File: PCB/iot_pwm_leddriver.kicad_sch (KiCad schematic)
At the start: 17 parts, among them J1 ProgConn-SOICBite, J2 12V PWR, SW1 RESET, SW2 FLASH, U2 ESP-12F

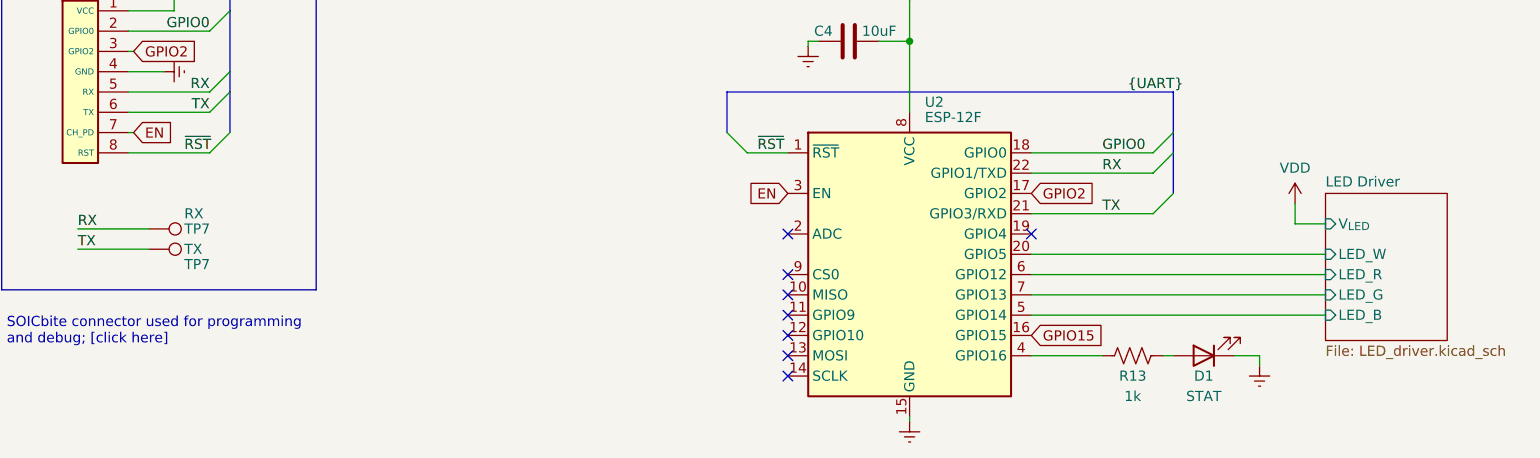
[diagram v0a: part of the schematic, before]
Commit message: design v1.0 - complete redesign
* redid schematic
* changed to screw terminal
* added W channel for RGBW strips
* did layout
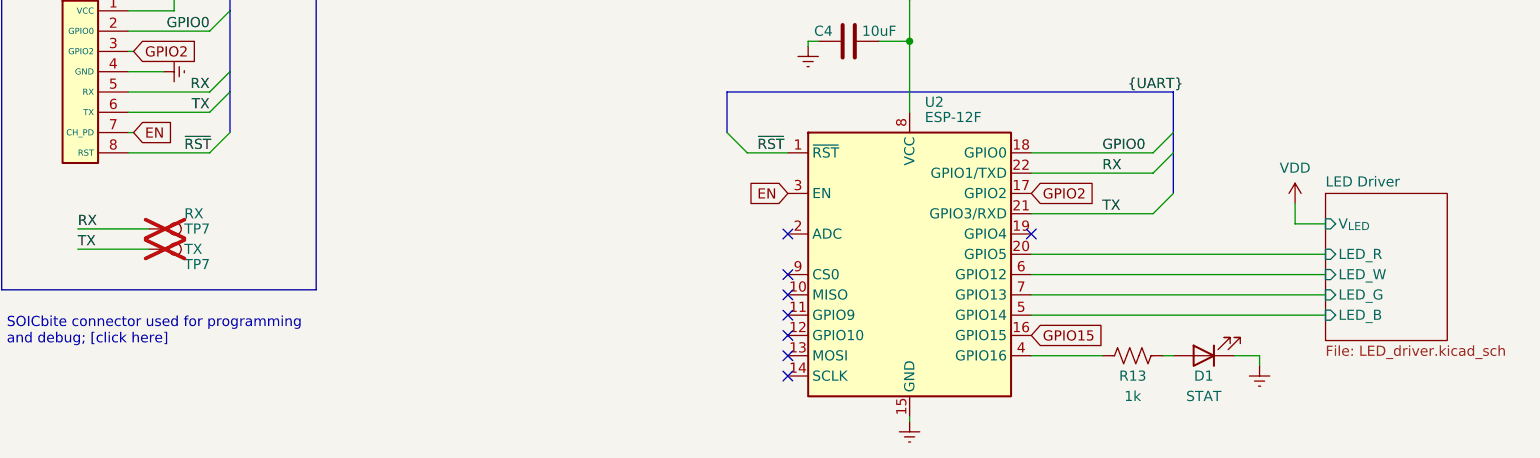
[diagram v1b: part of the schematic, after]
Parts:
- J1: LCSC (none) -> -
- R12, R13: LCSC (none) -> C17513
- TP7: LCSC (none) -> -; now not fitted
- U2: LCSC (none) -> C82891
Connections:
- net LED Driver/LED_R: now also U2.20 (GPIO5); no longer U2.6 (GPIO12)
- net LED Driver/LED_W: now also U2.6 (GPIO12); no longer U2.20 (GPIO5)
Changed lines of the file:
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@@
   )
   (symbol (lib_id "Connector:TestPoint") (at 38.1 113.03 270) (unit 1)
-    (in_bom no) (on_board yes) (dnp no)
+    (in_bom no) (on_board no) (dnp yes)
     (property "Reference" "TP7" (at 42.545 114.935 90)
       (effects (font (size 1.27 1.27)) (justify left))
@@
     )
     (property "Vendor" "~" (at 38.1 113.03 0)
+      (effects (font (size 1.27 1.27)) hide)
+    )
+    (property "Sim.Enable" "0" (at 38.1 113.03 0)
+      (effects (font (size 1.27 1.27)) hide)
+    )
+    (property "LCSC" "-" (at 38.1 113.03 0)
       (effects (font (size 1.27 1.27)) hide)
     )
@@
         )
       )
-      (project "dumb-led-driver"
+      (project "iot_pwm_leddriver"
         (path "/b6358773-9a18-4eb2-bc1b-d38393a8df39/ff2d7abe-3ed9-4cf8-a089-c3975f855094"
           (reference "TP2") (unit 1)
@@
         )
       )
-      (project "dumb-led-driver"
+      (project "iot_pwm_leddriver"
         (path "/b6358773-9a18-4eb2-bc1b-d38393a8df39"
           (reference "#PWR07") (unit 1)
@@
         )
       )
-      (project "dumb-led-driver"
+      (project "iot_pwm_leddriver"
         (path "/b6358773-9a18-4eb2-bc1b-d38393a8df39"
           (reference "#PWR01") (unit 1)
@@
         )
       )
-      (project "dumb-led-driver"
+      (project "iot_pwm_leddriver"
         (path "/b6358773-9a18-4eb2-bc1b-d38393a8df39"
           (reference "#PWR04") (unit 1)
@@
         )
       )
-      (project "dumb-led-driver"
+      (project "iot_pwm_leddriver"
         (path "/b6358773-9a18-4eb2-bc1b-d38393a8df39"
           (reference "#PWR05") (unit 1)
@@
         )
       )
-      (project "dumb-led-driver"
+      (project "iot_pwm_leddriver"
         (path "/b6358773-9a18-4eb2-bc1b-d38393a8df39"
           (reference "#PWR010") (unit 1)
@@
         )
       )
-      (project "dumb-led-driver"
+      (project "iot_pwm_leddriver"
         (path "/b6358773-9a18-4eb2-bc1b-d38393a8df39"
           (reference "#PWR014") (unit 1)
@@
         )
       )
-      (project "dumb-led-driver"
+      (project "iot_pwm_leddriver"
         (path "/b6358773-9a18-4eb2-bc1b-d38393a8df39"
           (reference "D2") (unit 1)
@@
         )
       )
-      (project "dumb-led-driver"
+      (project "iot_pwm_leddriver"
         (path "/b6358773-9a18-4eb2-bc1b-d38393a8df39"
           (reference "#PWR03") (unit 1)
@@
     (pin "1")
     (instances
-      (project "dumb-led-driver"
+      (project "iot_pwm_leddriver"
         (path "/b6358773-9a18-4eb2-bc1b-d38393a8df39"
           (reference "#PWR023") (unit 1)
@@
         )
       )
-      (project "dumb-led-driver"
+      (project "iot_pwm_leddriver"
         (path "/b6358773-9a18-4eb2-bc1b-d38393a8df39"
           (reference "#PWR06") (unit 1)
@@
         )
       )
-      (project "dumb-led-driver"
+      (project "iot_pwm_leddriver"
         (path "/b6358773-9a18-4eb2-bc1b-d38393a8df39"
           (reference "#PWR02") (unit 1)
@@
         )
       )
-      (project "dumb-led-driver"
+      (project "iot_pwm_leddriver"
         (path "/b6358773-9a18-4eb2-bc1b-d38393a8df39"
           (reference "#PWR019") (unit 1)
@@
         )
       )
-      (project "dumb-led-driver"
+      (project "iot_pwm_leddriver"
         (path "/b6358773-9a18-4eb2-bc1b-d38393a8df39"
           (reference "R5") (unit 1)
@@
         )
       )
-      (project "dumb-led-driver"
+      (project "iot_pwm_leddriver"
         (path "/b6358773-9a18-4eb2-bc1b-d38393a8df39"
           (reference "#PWR018") (unit 1)
@@
         )
       )
-      (project "dumb-led-driver"
+      (project "iot_pwm_leddriver"
         (path "/b6358773-9a18-4eb2-bc1b-d38393a8df39"
           (reference "J2") (unit 1)
@@
         )
       )
-      (project "dumb-led-driver"
+      (project "iot_pwm_leddriver"
         (path "/b6358773-9a18-4eb2-bc1b-d38393a8df39"
           (reference "SW1") (unit 1)
@@
         )
       )
-      (project "dumb-led-driver"
+      (project "iot_pwm_leddriver"
         (path "/b6358773-9a18-4eb2-bc1b-d38393a8df39"
           (reference "#PWR017") (unit 1)
@@
         )
       )
-      (project "dumb-led-driver"
+      (project "iot_pwm_leddriver"
         (path "/b6358773-9a18-4eb2-bc1b-d38393a8df39"
           (reference "#PWR021") (unit 1)
@@
         )
       )
-      (project "dumb-led-driver"
+      (project "iot_pwm_leddriver"
         (path "/b6358773-9a18-4eb2-bc1b-d38393a8df39"
           (reference "R2") (unit 1)
@@
         )
       )
-      (project "dumb-led-driver"
+      (project "iot_pwm_leddriver"
         (path "/b6358773-9a18-4eb2-bc1b-d38393a8df39"
           (reference "R3") (unit 1)
@@
         )
       )
-      (project "dumb-led-driver"
+      (project "iot_pwm_leddriver"
         (path "/b6358773-9a18-4eb2-bc1b-d38393a8df39"
           (reference "#PWR09") (unit 1)
@@
         )
       )
-      (project "dumb-led-driver"
+      (project "iot_pwm_leddriver"
         (path "/b6358773-9a18-4eb2-bc1b-d38393a8df39"
           (reference "SW2") (unit 1)
@@
       (effects (font (size 1.27 1.27)) hide)
     )
-    (property "LCSC" "" (at 161.29 126.365 0)
+    (property "LCSC" " C17513 " (at 161.29 126.365 0)
+      (effects (font (size 1.27 1.27)) hide)
+    )
+    (property "Description" "125mW Thick Film Resistors ±100ppm/℃ ±1% 1kΩ 0805 Chip Resistor - Surface Mount ROHS" (at 161.29 126.365 0)
       (effects (font (size 1.27 1.27)) hide)
     )
@@
         )
       )
-      (project "dumb-led-driver"
+      (project "iot_pwm_leddriver"
         (path "/b6358773-9a18-4eb2-bc1b-d38393a8df39"
           (reference "R9") (unit 1)
@@
         )
       )
-      (project "dumb-led-driver"
+      (project "iot_pwm_leddriver"
         (path "/b6358773-9a18-4eb2-bc1b-d38393a8df39"
           (reference "R1") (unit 1)
@@
         )
       )
-      (project "dumb-led-driver"
+      (project "iot_pwm_leddriver"
         (path "/b6358773-9a18-4eb2-bc1b-d38393a8df39"
           (reference "#PWR08") (unit 1)
@@
     )
     (property "Datasheet" "http://wiki.ai-thinker.com/_media/esp8266/esp8266_series_modules_user_manual_v1.1.pdf" (at 124.46 113.665 0)
+      (effects (font (size 1.27 1.27)) hide)
+    )
+    (property "LCSC" " C82891 " (at 133.35 116.205 0)
       (effects (font (size 1.27 1.27)) hide)
     )
@@
         )
       )
-      (project "dumb-led-driver"
+      (project "iot_pwm_leddriver"
         (path "/b6358773-9a18-4eb2-bc1b-d38393a8df39"
           (reference "U1") (unit 1)
@@
   )
   (symbol (lib_id "Connector:TestPoint") (at 38.1 110.49 270) (unit 1)
-    (in_bom no) (on_board yes) (dnp no)
+    (in_bom no) (on_board no) (dnp yes)
     (property "Reference" "TP7" (at 42.545 110.49 90)
       (effects (font (size 1.27 1.27)) (justify left))
@@
     )
     (property "Vendor" "~" (at 38.1 110.49 0)
+      (effects (font (size 1.27 1.27)) hide)
+    )
+    (property "Sim.Enable" "0" (at 38.1 110.49 0)
+      (effects (font (size 1.27 1.27)) hide)
+    )
+    (property "LCSC" "-" (at 38.1 110.49 0)
       (effects (font (size 1.27 1.27)) hide)
     )
@@
         )
       )
-      (project "dumb-led-driver"
+      (project "iot_pwm_leddriver"
         (path "/b6358773-9a18-4eb2-bc1b-d38393a8df39/ff2d7abe-3ed9-4cf8-a089-c3975f855094"
           (reference "TP1") (unit 1)
@@
         )
       )
-      (project "dumb-led-driver"
+      (project "iot_pwm_leddriver"
         (path "/b6358773-9a18-4eb2-bc1b-d38393a8df39"
           (reference "R4") (unit 1)
@@
         )
       )
-      (project "dumb-led-driver"
+      (project "iot_pwm_leddriver"
         (path "/b6358773-9a18-4eb2-bc1b-d38393a8df39"
           (reference "D1") (unit 1)
@@
         )
       )
-      (project "dumb-led-driver"
+      (project "iot_pwm_leddriver"
         (path "/b6358773-9a18-4eb2-bc1b-d38393a8df39"
           (reference "C1") (unit 1)
@@
       (effects (font (size 1.27 1.27)) hide)
     )
-    (property "LCSC" "" (at 93.345 34.925 0)
+    (property "LCSC" " C17513 " (at 93.345 34.925 0)
+      (effects (font (size 1.27 1.27)) hide)
+    )
+    (property "Description" "125mW Thick Film Resistors ±100ppm/℃ ±1% 1kΩ 0805 Chip Resistor - Surface Mount ROHS" (at 93.345 34.925 0)
       (effects (font (size 1.27 1.27)) hide)
     )
@@
         )
       )
-      (project "dumb-led-driver"
+      (project "iot_pwm_leddriver"
         (path "/b6358773-9a18-4eb2-bc1b-d38393a8df39"
           (reference "R6") (unit 1)
@@
     )
     (property "Datasheet" "" (at 38.1 104.775 0)
+      (effects (font (size 1.27 1.27)) hide)
+    )
+    (property "LCSC" "-" (at 38.1 104.775 0)
       (effects (font (size 1.27 1.27)) hide)
     )
@@
     (pin "8")
     (instances
-      (project "dumb-led-driver"
+      (project "iot_pwm_leddriver"
         (path "/b6358773-9a18-4eb2-bc1b-d38393a8df39"
           (reference "J1") (unit 1)
@@
       (effects (font (size 1.27 1.27)) (justify left))
     )
-    (pin "LED_R" input (at 185.42 116.205 180)
+    (pin "LED_R" input (at 185.42 113.665 180)
       (effects (font (size 1.27 1.27)) (justify left))
     )
@@
       (effects (font (size 1.27 1.27)) (justify left))
     )
-    (pin "LED_W" input (at 185.42 113.665 180)
-      (effects (font (size 1.27 1.27)) (justify left))
-    )
-    (instances
-      (project "dumb-led-driver"
+    (pin "LED_W" input (at 185.42 116.205 180)
+      (effects (font (size 1.27 1.27)) (justify left))
+    )
+    (instances
+      (project "iot_pwm_leddriver"
         (path "/b6358773-9a18-4eb2-bc1b-d38393a8df39" (page "2"))
       )
@@
     )
     (instances
-      (project "dumb-led-driver"
+      (project "iot_pwm_leddriver"
         (path "/b6358773-9a18-4eb2-bc1b-d38393a8df39" (page "3"))
       )

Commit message: schematic and layout cleanup
* plus BOM finalization
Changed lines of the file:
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@@
     (fill (color 255 229 191 1.0000))
     (property "Sheetname" "LED Driver" (at 185.42 105.3334 0)
-      (effects (font (size 1.27 1.27)) (justify left bottom))
+      (effects (font (size 1.27 1.27) bold) (justify left bottom))
     )
     (property "Sheetfile" "LED_driver.kicad_sch" (at 185.42 125.0446 0)
@@
     (fill (color 255 229 191 1.0000))
     (property "Sheetname" "Power_and_board" (at 48.895 27.2284 0)
-      (effects (font (size 1.27 1.27)) (justify left bottom))
+      (effects (font (size 1.27 1.27) bold) (justify left bottom))
     )
     (property "Sheetfile" "Power_and_board.kicad_sch" (at 48.895 36.1446 0)
